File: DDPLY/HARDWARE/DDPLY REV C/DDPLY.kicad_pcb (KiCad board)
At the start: 2 copper layers, 31.1 x 25.8 mm, 63 parts, among them P1 USB_OTG, P2 PWR, P3 SW, P4 E-MATCH_1, P5 ICSP, P6 E-MATCH_2, P7 PIEZO, Q1 Q_NJFET_GSD, Q2 Q_NJFET_GSD, Q3 Q_NJFET_GSD, U1 AP2210, U2 FT230XQ-R, U4 BMP280, U5 ATTINY841-MMH

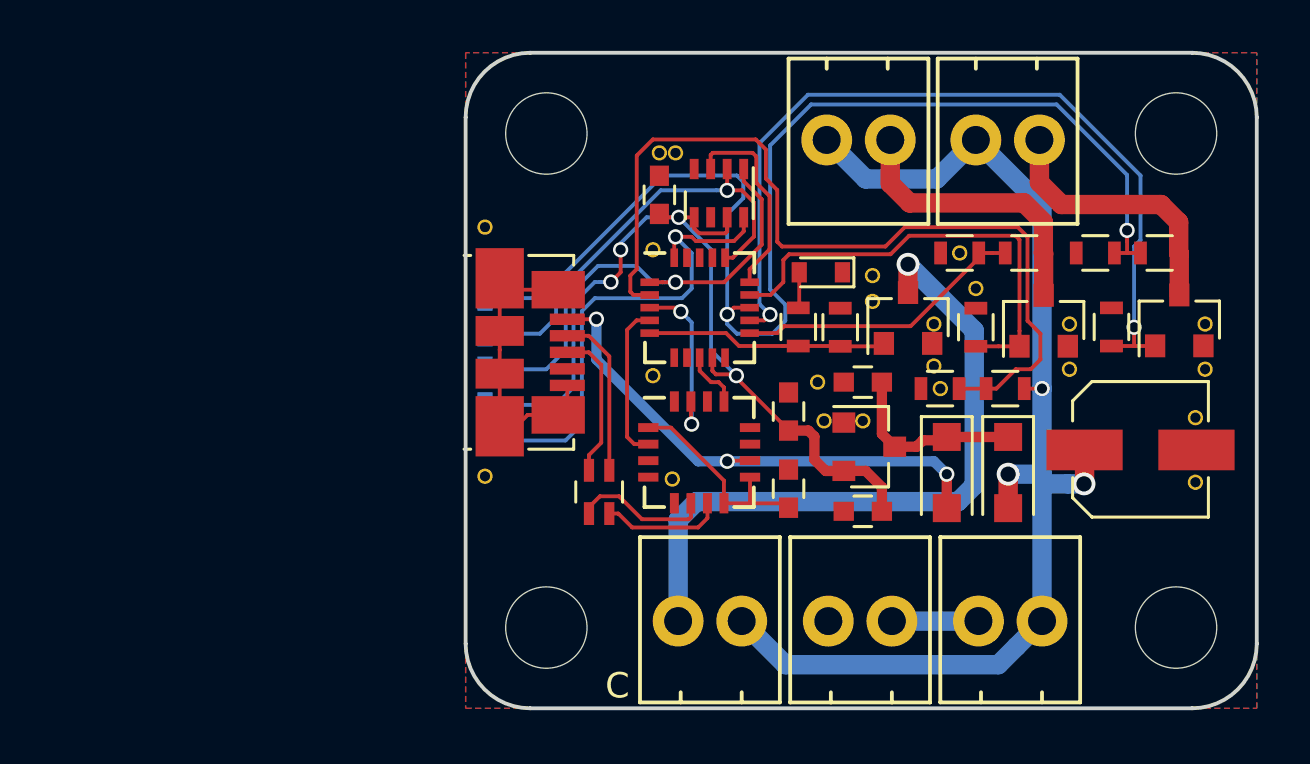
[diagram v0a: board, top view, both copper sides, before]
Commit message: LWRA BOM fix
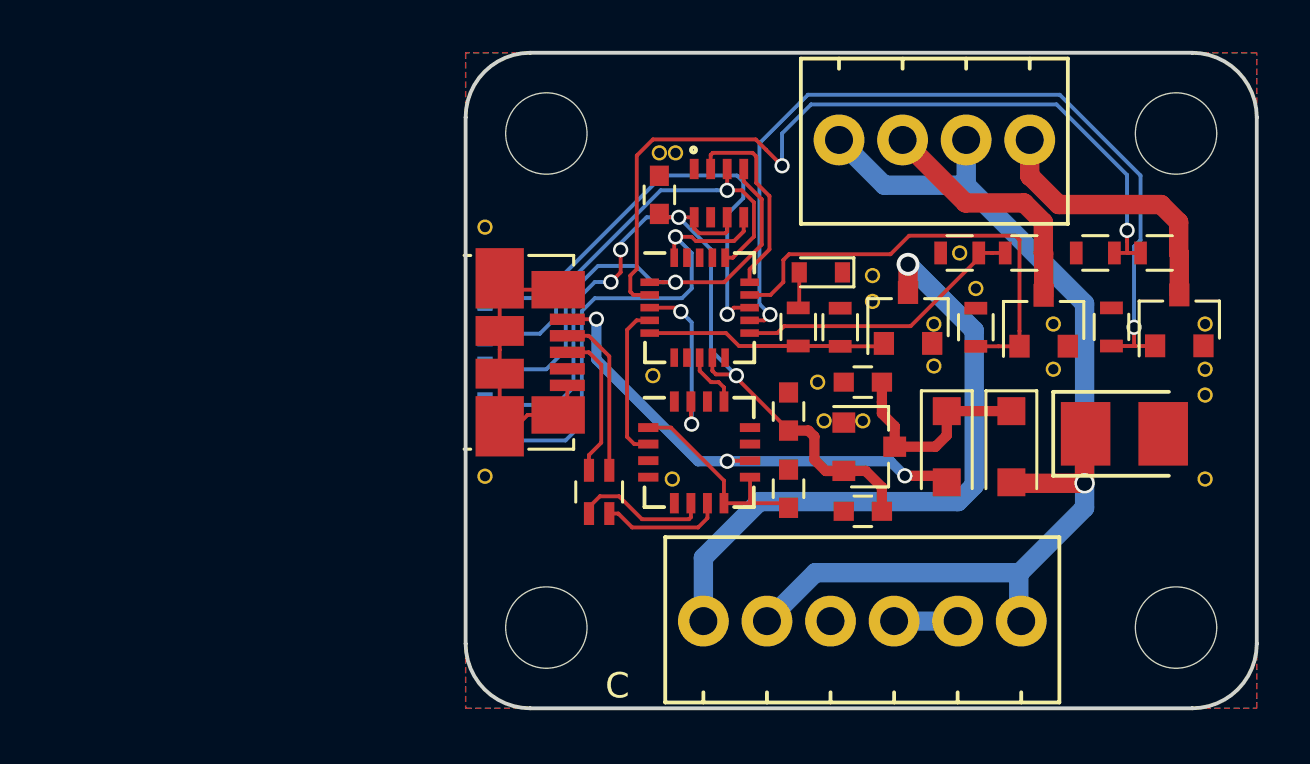
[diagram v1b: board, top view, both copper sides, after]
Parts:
- removed the ? at (153.0, 97.4)
- removed the ? at (164.3, 102.9)
- removed P4: E-MATCH_1, MOD:100MIL_ST
- removed P6: E-MATCH_2, MOD:100MIL_ST
- removed P7: PIEZO, MOD:100MIL_ST
- removed R5: 10K, Resistors_SMD:R_0603
- removed R6: 2K, Resistors_SMD:R_0603
- C1, C2, C3, C4, C8: value C -> 1uF
- C6: footprint Capacitors_SMD:CP_Elec_5x5.3 -> Capacitors_Tantalum_SMD:Tantalum_Case-B_EIA-3528-21_Reflow
- P2: value PWR -> SCREW; footprint MOD:100MIL_ST -> MOD:100MIL_STX4
- P3: value SW -> SCREW; footprint MOD:100MIL_ST -> MOD:100MIL_STX6
- U4: footprint MOD:LGA-8_NO_DOT -> MOD:LGA-8_PIN1_DOT
- moved P2 13.3 mm to (169.4, 97.7), turned to 180 degrees
- moved P3 4.91 mm to (153.5, 110.0)
- moved G*** 1.91 mm to (157.2, 100.5)
- moved D1 1.02 mm to (167.1, 106.4)
- moved D2 1.02 mm to (164.6, 106.4)
- moved ? 0.97 mm to (174.8, 103.1)
- moved C6 0.90 mm to (171.6, 105.9)
- moved ? 0.64 mm to (168.8, 102.1)
- moved ? 0.64 mm to (168.8, 100.3)
- moved ? 0.40 mm to (174.8, 106.4)
- moved G*** 0.13 mm to (152.3, 109.0)
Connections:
- P2 pad 1: Net-(P2-Pad1) -> E-M2
- P3 pad 1: GND -> PIEZO_OUT
- P3 pad 2: Net-(P2-Pad1) -> +9V
- P5 pad 5: CONT_2 -> RST_AVR
- Q1 pad 3: Net-(P4-Pad1) -> E-M1
- Q2 pad 3: Net-(P6-Pad1) -> E-M2
- Q3 pad 3: Net-(P7-Pad1) -> PIEZO_OUT
- R10 pad 1: Net-(P4-Pad1) -> E-M1
- R12 pad 1: Net-(P6-Pad1) -> E-M2
- U5 pad 13: CONT_2 -> RST_AVR
- U5 pad 2: 9V/6 -> CONT_2
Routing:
- net 9V/6: track 34.7 -> 0.00 mm
- net Net-(P7-Pad1): track 27.1 -> 0.00 mm, vias 1 -> 0
- net PIEZO_OUT: track 0.00 -> 25.2 mm, vias 0 -> 1
- net RST_AVR: track 0.00 -> 18.7 mm, vias 0 -> 1
- net CONT_2: track 48.9 -> 33.2 mm
- net Net-(P4-Pad1): track 11.2 -> 0.00 mm
- net E-M2: track 0.00 -> 10.9 mm
- net Net-(P6-Pad1): track 10.7 -> 0.00 mm
- net E-M1: track 0.00 -> 9.76 mm
- net +9V: track 46.7 -> 42.6 mm, vias 3 -> 1
- net Net-(P2-Pad1): track 3.41 -> 0.00 mm
- net Net-(P3-Pad4): track 0.00 -> 2.50 mm
- net +5V: track 20.6 -> 19.4 mm
- net Net-(C3-Pad1): track 7.37 -> 8.48 mm

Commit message: added gate resistors DDPLY
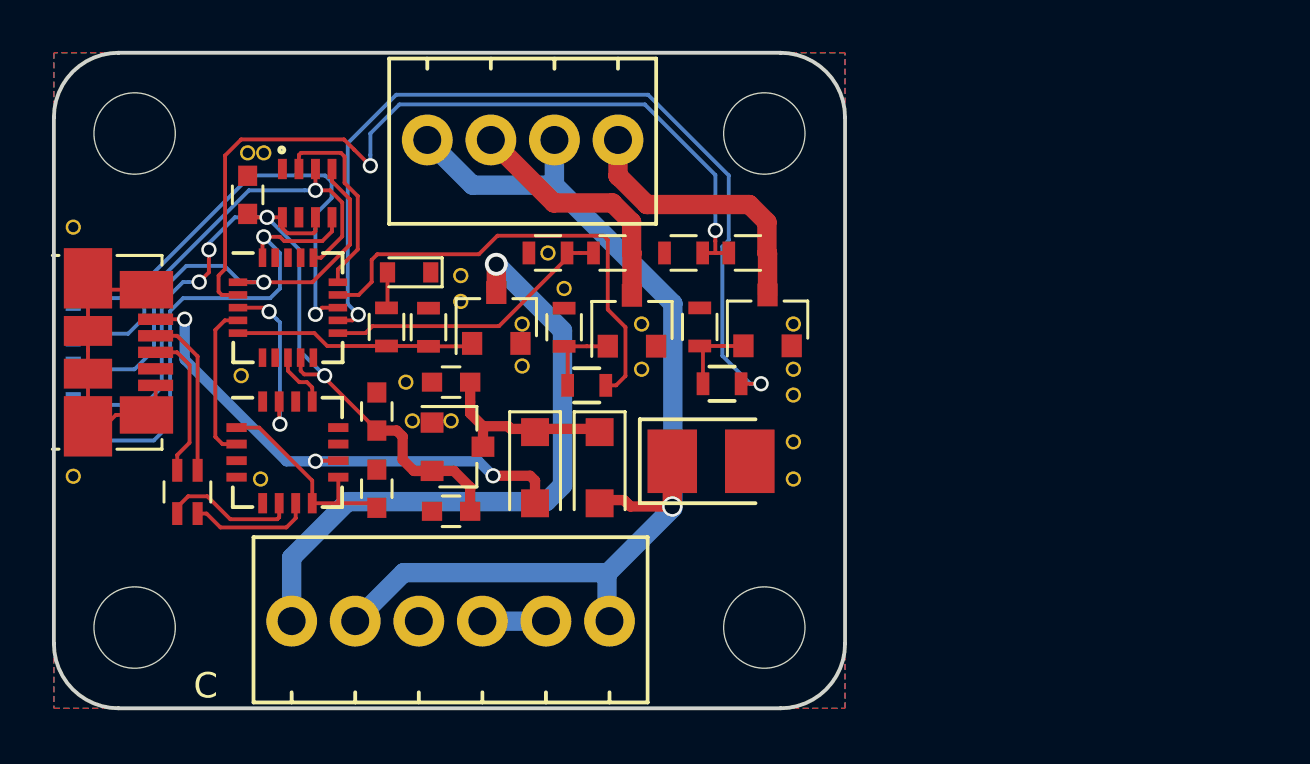
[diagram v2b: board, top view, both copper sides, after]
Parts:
- added ?: , MOD:GND VIA, F.Cu at (158.6, 105.0)
- added R3: 680, Resistors_SMD:R_0603, F.Cu at (150.4, 104.0)
- added R4: 680, Resistors_SMD:R_0603, F.Cu at (155.8, 103.9)
- R2: value 330 -> 680
- moved C6 16.3 mm to (155.3, 107.0)
- moved D2 16.2 mm to (148.4, 107.3)
- moved D1 16.2 mm to (150.9, 107.3)
- moved ? 16.2 mm to (149.5, 98.9)
- moved ? 16.2 mm to (130.2, 106.3)
- moved ? 16.2 mm to (130.2, 96.5)
- moved D3 16.2 mm to (143.4, 99.6)
- moved P2 16.2 mm to (153.2, 97.7)
- moved P3 16.2 mm to (137.3, 110.0)
- moved Q3 16.2 mm to (146.9, 101.4)
- moved R7 16.2 mm to (149.5, 101.7)
- moved R9 16.2 mm to (144.2, 101.7)
- moved U1 16.2 mm to (145.4, 106.4)
- moved U2 16.2 mm to (138.7, 106.6)
- moved ? 16.2 mm to (158.6, 103.1)
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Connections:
- Q1 pad 1: E-MATCH_1 -> Net-(Q1-Pad1)
- Q2 pad 1: E-MATCH_2 -> Net-(Q2-Pad1)
- R7 pad 1: E-MATCH_1 -> Net-(Q1-Pad1)
- R8 pad 1: E-MATCH_2 -> Net-(Q2-Pad1)
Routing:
- net Net-(Q1-Pad1): track 0.00 -> 3.31 mm
- net Net-(Q2-Pad1): track 0.00 -> 3.26 mm
- net E-MATCH_2: track 33.4 -> 34.9 mm
- net Net-(C3-Pad1): track 8.48 -> 7.38 mm
- net +5V: track 19.4 -> 20.2 mm
- net E-MATCH_1: track 18.1 -> 18.7 mm
